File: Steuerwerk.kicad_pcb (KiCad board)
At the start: 2 copper layers, 100 x 160 mm, 116 parts, among them J1 Conn_01x04, J2 Conn_01x02, J3 Conn_01x03, J4 Conn_01x03, J5 Conn_01x02, J6 Conn_01x04, J7 Conn_01x02, J8 Conn_01x04, J9 Conn_01x02, Q1 Q_PNP_BCE, U1 74LS161, U2 74LS138, U3 74LS138, U4 74240, U5 74LS374, U6 74LS374, U7 74541, U8 74541

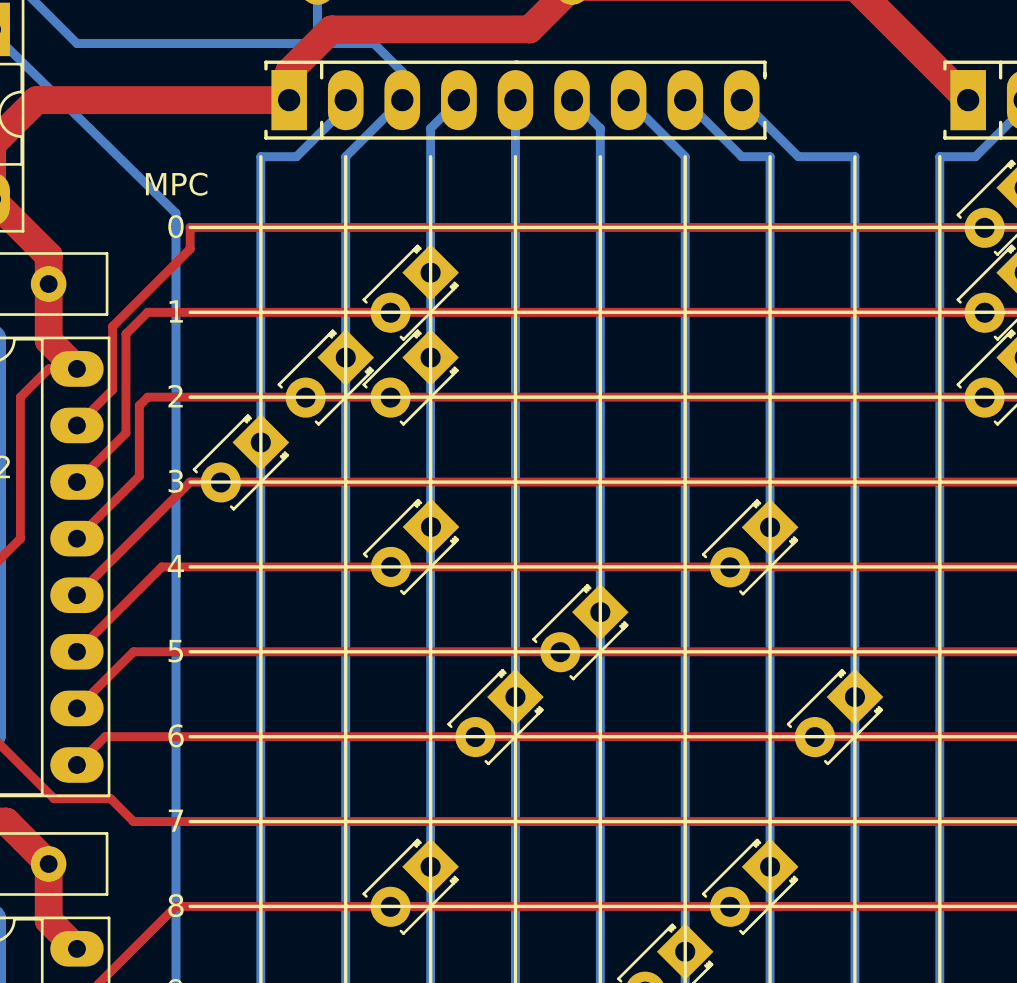
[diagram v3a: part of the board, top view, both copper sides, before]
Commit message: Steuerwerk: Platzhalter für LEDs eingefügt
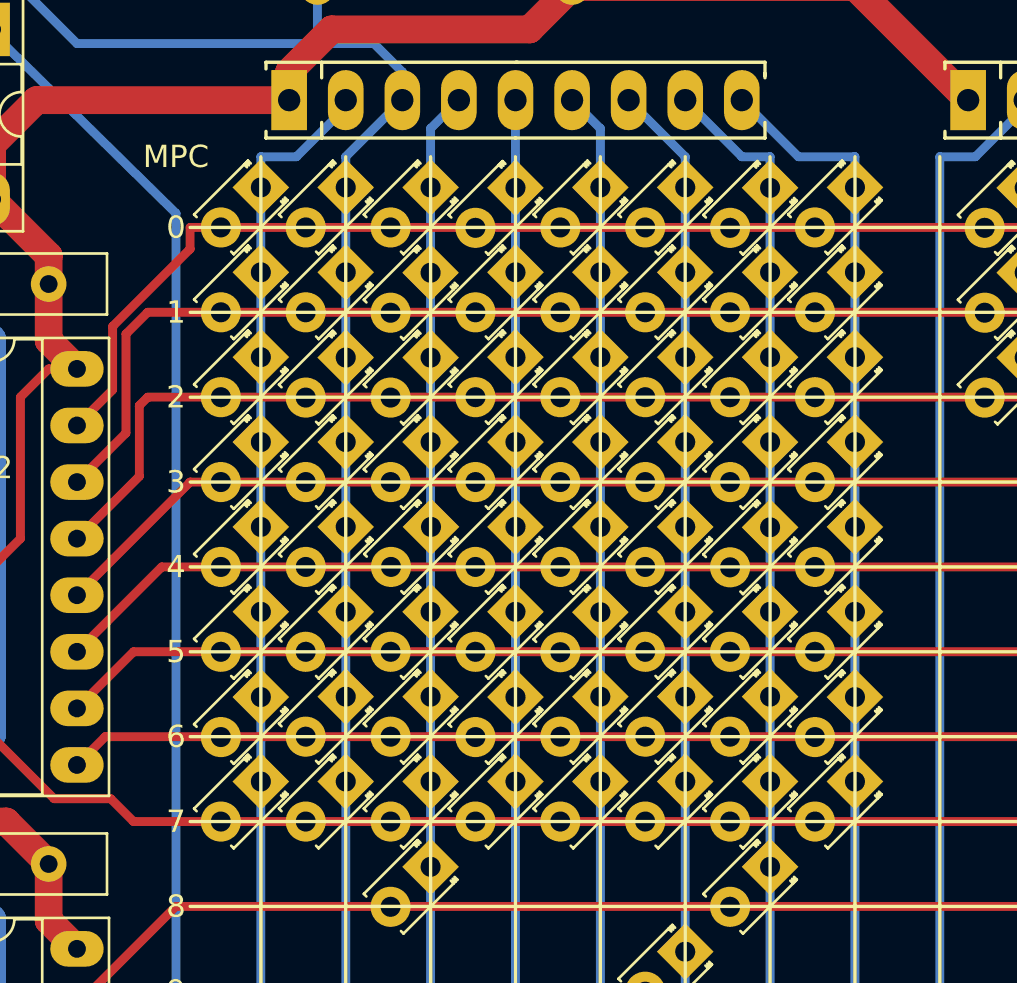
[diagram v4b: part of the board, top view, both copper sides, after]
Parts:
- added D100: bonsai_Led_Small_Platzhalter, bonsai:LED_Diodenmatrix_Platzhalter, F.Cu at (85.1, 75.6)
- added D101: bonsai_Led_Small_Platzhalter, bonsai:LED_Diodenmatrix_Platzhalter, F.Cu at (88.9, 75.6)
- added D102: bonsai_Led_Small_Platzhalter, bonsai:LED_Diodenmatrix_Platzhalter, F.Cu at (92.7, 75.6)
- added D103: bonsai_Led_Small_Platzhalter, bonsai:LED_Diodenmatrix_Platzhalter, F.Cu at (100.4, 75.6)
- added D104: bonsai_Led_Small_Platzhalter, bonsai:LED_Diodenmatrix_Platzhalter, F.Cu at (104.2, 75.6)
- added D105: bonsai_Led_Small_Platzhalter, bonsai:LED_Diodenmatrix_Platzhalter, F.Cu at (108.0, 75.6)
- added D106: bonsai_Led_Small_Platzhalter, bonsai:LED_Diodenmatrix_Platzhalter, F.Cu at (85.1, 79.4)
- added D107: bonsai_Led_Small_Platzhalter, bonsai:LED_Diodenmatrix_Platzhalter, F.Cu at (88.9, 79.4)
- added D108: bonsai_Led_Small_Platzhalter, bonsai:LED_Diodenmatrix_Platzhalter, F.Cu at (96.6, 79.4)
- added D109: bonsai_Led_Small_Platzhalter, bonsai:LED_Diodenmatrix_Platzhalter, F.Cu at (100.4, 79.4)
- added D110: bonsai_Led_Small_Platzhalter, bonsai:LED_Diodenmatrix_Platzhalter, F.Cu at (104.2, 79.4)
- added D111: bonsai_Led_Small_Platzhalter, bonsai:LED_Diodenmatrix_Platzhalter, F.Cu at (81.3, 83.3)
- added D112: bonsai_Led_Small_Platzhalter, bonsai:LED_Diodenmatrix_Platzhalter, F.Cu at (85.1, 83.3)
- added D113: bonsai_Led_Small_Platzhalter, bonsai:LED_Diodenmatrix_Platzhalter, F.Cu at (88.9, 83.3)
- added D114: bonsai_Led_Small_Platzhalter, bonsai:LED_Diodenmatrix_Platzhalter, F.Cu at (92.7, 83.3)
- added D115: bonsai_Led_Small_Platzhalter, bonsai:LED_Diodenmatrix_Platzhalter, F.Cu at (96.6, 83.3)
- added D116: bonsai_Led_Small_Platzhalter, bonsai:LED_Diodenmatrix_Platzhalter, F.Cu at (100.4, 83.3)
- added D117: bonsai_Led_Small_Platzhalter, bonsai:LED_Diodenmatrix_Platzhalter, F.Cu at (104.2, 83.3)
- added D118: bonsai_Led_Small_Platzhalter, bonsai:LED_Diodenmatrix_Platzhalter, F.Cu at (108.0, 83.3)
- added D64: bonsai_Led_Small_Platzhalter, bonsai:LED_Diodenmatrix_Platzhalter, F.Cu at (81.3, 56.6)
- added D65: bonsai_Led_Small_Platzhalter, bonsai:LED_Diodenmatrix_Platzhalter, F.Cu at (85.1, 56.6)
- added D66: bonsai_Led_Small_Platzhalter, bonsai:LED_Diodenmatrix_Platzhalter, F.Cu at (88.9, 56.6)
- added D67: bonsai_Led_Small_Platzhalter, bonsai:LED_Diodenmatrix_Platzhalter, F.Cu at (92.7, 56.6)
- added D68: bonsai_Led_Small_Platzhalter, bonsai:LED_Diodenmatrix_Platzhalter, F.Cu at (96.6, 56.6)
- added D69: bonsai_Led_Small_Platzhalter, bonsai:LED_Diodenmatrix_Platzhalter, F.Cu at (100.4, 56.6)
- added D70: bonsai_Led_Small_Platzhalter, bonsai:LED_Diodenmatrix_Platzhalter, F.Cu at (104.2, 56.6)
- added D71: bonsai_Led_Small_Platzhalter, bonsai:LED_Diodenmatrix_Platzhalter, F.Cu at (108.0, 56.6)
- added D72: bonsai_Led_Small_Platzhalter, bonsai:LED_Diodenmatrix_Platzhalter, F.Cu at (81.3, 60.4)
- added D73: bonsai_Led_Small_Platzhalter, bonsai:LED_Diodenmatrix_Platzhalter, F.Cu at (85.1, 60.4)
- added D74: bonsai_Led_Small_Platzhalter, bonsai:LED_Diodenmatrix_Platzhalter, F.Cu at (92.7, 60.4)
- added D75: bonsai_Led_Small_Platzhalter, bonsai:LED_Diodenmatrix_Platzhalter, F.Cu at (96.6, 60.4)
- added D76: bonsai_Led_Small_Platzhalter, bonsai:LED_Diodenmatrix_Platzhalter, F.Cu at (100.4, 60.4)
- added D77: bonsai_Led_Small_Platzhalter, bonsai:LED_Diodenmatrix_Platzhalter, F.Cu at (104.2, 60.4)
- added D78: bonsai_Led_Small_Platzhalter, bonsai:LED_Diodenmatrix_Platzhalter, F.Cu at (108.0, 60.4)
- added D79: bonsai_Led_Small_Platzhalter, bonsai:LED_Diodenmatrix_Platzhalter, F.Cu at (81.3, 64.2)
- added D80: bonsai_Led_Small_Platzhalter, bonsai:LED_Diodenmatrix_Platzhalter, F.Cu at (92.7, 64.2)
- added D81: bonsai_Led_Small_Platzhalter, bonsai:LED_Diodenmatrix_Platzhalter, F.Cu at (96.6, 64.2)
- added D82: bonsai_Led_Small_Platzhalter, bonsai:LED_Diodenmatrix_Platzhalter, F.Cu at (100.4, 64.2)
- added D83: bonsai_Led_Small_Platzhalter, bonsai:LED_Diodenmatrix_Platzhalter, F.Cu at (104.2, 64.2)
- added D84: bonsai_Led_Small_Platzhalter, bonsai:LED_Diodenmatrix_Platzhalter, F.Cu at (108.0, 64.2)
- added D85: bonsai_Led_Small_Platzhalter, bonsai:LED_Diodenmatrix_Platzhalter, F.Cu at (81.3, 68.0)
- added D86: bonsai_Led_Small_Platzhalter, bonsai:LED_Diodenmatrix_Platzhalter, F.Cu at (85.1, 68.0)
- added D87: bonsai_Led_Small_Platzhalter, bonsai:LED_Diodenmatrix_Platzhalter, F.Cu at (88.9, 68.0)
- added D88: bonsai_Led_Small_Platzhalter, bonsai:LED_Diodenmatrix_Platzhalter, F.Cu at (92.7, 68.0)
- added D89: bonsai_Led_Small_Platzhalter, bonsai:LED_Diodenmatrix_Platzhalter, F.Cu at (96.6, 68.0)
- added D90: bonsai_Led_Small_Platzhalter, bonsai:LED_Diodenmatrix_Platzhalter, F.Cu at (100.4, 68.0)
- added D91: bonsai_Led_Small_Platzhalter, bonsai:LED_Diodenmatrix_Platzhalter, F.Cu at (104.2, 68.0)
- added D92: bonsai_Led_Small_Platzhalter, bonsai:LED_Diodenmatrix_Platzhalter, F.Cu at (108.0, 68.0)
- added D93: bonsai_Led_Small_Platzhalter, bonsai:LED_Diodenmatrix_Platzhalter, F.Cu at (81.3, 71.8)
- added D94: bonsai_Led_Small_Platzhalter, bonsai:LED_Diodenmatrix_Platzhalter, F.Cu at (85.1, 71.8)
- added D95: bonsai_Led_Small_Platzhalter, bonsai:LED_Diodenmatrix_Platzhalter, F.Cu at (92.7, 71.8)
- added D96: bonsai_Led_Small_Platzhalter, bonsai:LED_Diodenmatrix_Platzhalter, F.Cu at (96.6, 71.8)
- added D97: bonsai_Led_Small_Platzhalter, bonsai:LED_Diodenmatrix_Platzhalter, F.Cu at (100.4, 71.8)
- added D98: bonsai_Led_Small_Platzhalter, bonsai:LED_Diodenmatrix_Platzhalter, F.Cu at (108.0, 71.8)
- added D99: bonsai_Led_Small_Platzhalter, bonsai:LED_Diodenmatrix_Platzhalter, F.Cu at (81.3, 75.6)
- moved D10 11.4 mm to (81.3, 79.5)
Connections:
- D10 pad 2: /h3 -> /h6
